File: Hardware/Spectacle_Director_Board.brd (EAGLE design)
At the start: 25.4 x 55.9 mm, 57 parts, among them J1 AUDIO-JACK3, J2 CORTEX_DEBUGPTH, Q1 2N7002PW, Q2 2N7002PW, U3 AP2112K-3.3V, U4 ATSAMD21G-A, U5 W25Q32FVSS

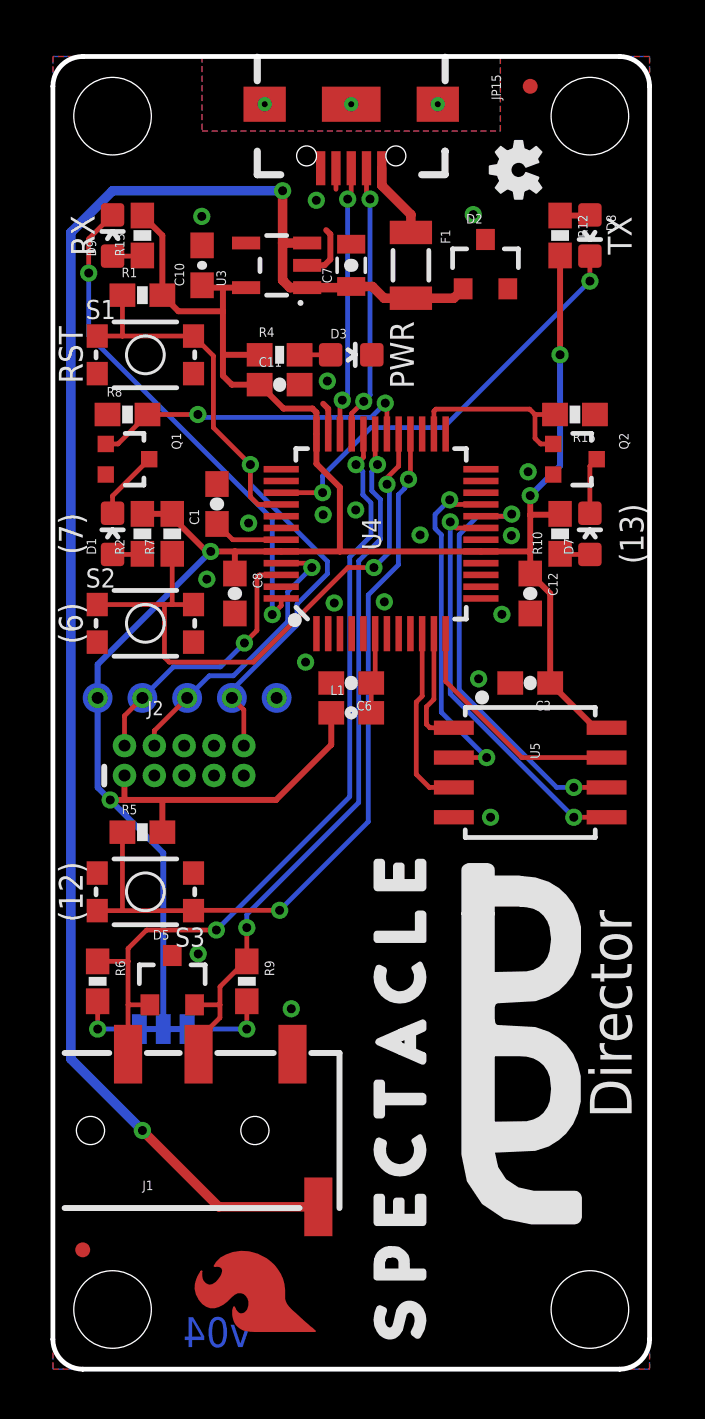
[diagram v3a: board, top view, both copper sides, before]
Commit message: Adding second trrs for program, usb out control
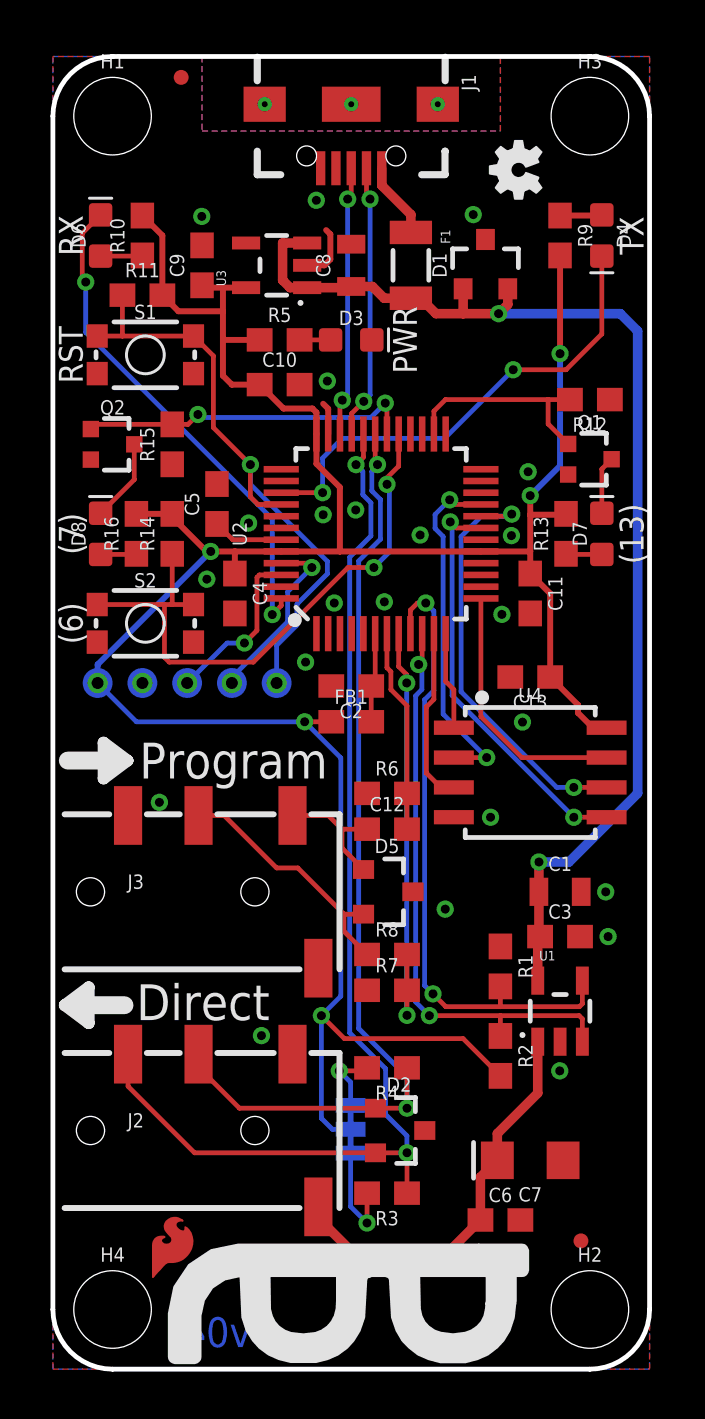
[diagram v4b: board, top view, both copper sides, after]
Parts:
- removed D9: Yellow, SparkFun-LED:LED-0603
- removed JP15: (no value), SparkFun-Connectors:USB-B-MICRO-SMD_V03
- removed JP2: JUMPER-SMT_3_2-NC_TRACE_SILK, SparkFun-Jumpers:SMT-JUMPER_3_2-NC_TRACE_SILK
- removed L1: FB - 30Ohm, SparkFun-Passives:0603
- removed S3: BTN1, SparkFun-Electromechanical:TACTILE_SWITCH_SMD_4.6X2.8MM
- removed U5: W25Q32FVSS, SparkFun-DigitalIC:SOIC-8
- added C13, C3, C4, C5: 0.1uF, SparkFun-Capacitors:0603
- added C9: 2.2uF, SparkFun-Capacitors:0603
- added D4: GREEN, SparkFun-LED:LED-0603
- added D6: Yellow, SparkFun-LED:LED-0603
- added FB1: 30Ω/1.8A, SparkFun-Inductors:0603
- added J3: Serial-TRRS, SparkFun-Connectors:AUDIO_JACK_3.5MM_TRRS_SMD_RA
- added JP1: JUMPER-SMT_3_2-NC_TRACE_SILK, SparkFun-Jumpers:SMT-JUMPER_3_2-NC_TRACE_SILK
- added R11, R14: 10k, SparkFun-Resistors:0603
- added R16: 330, SparkFun-Resistors:0603
- added R3: 2.2k, SparkFun-Resistors:0603
- added U1: AP2151, spectacle-director-temp:SOT23-5
- added U2: ATSAMD21G-A, SparkFun-IC-Microcontroller:TQFP-48
- C1: value 0.1uF -> 10uF; device SparkFun-Capacitors:0603-CAP -> SparkFun-Capacitors:0805
- C10: value 2.2uF -> 0.1uF; device SparkFun-Capacitors:0603-CAP@1 -> SparkFun-Capacitors:0603
- C11, C2, C6: device SparkFun-Capacitors:0603-CAP -> SparkFun-Capacitors:0603
- C12: value 0.1uF -> 1.0uF; device SparkFun-Capacitors:0603-CAP -> SparkFun-Capacitors:0603
- C7: value 1.0uF -> 10uF; device SparkFun-Capacitors:0805-CAP -> SparkFun-Capacitors:EIA3216
- C8: value 0.1uF -> 1.0uF; device SparkFun-Capacitors:0603-CAP -> SparkFun-Capacitors:0805
- D1: value GREEN -> PESD1CAN; device SparkFun-LED:LED-0603 -> SparkFun-DiscreteSemi:SOT23-3
- FD1, FD2: device SparkFun-Aesthetics:MICRO-FIDUCIAL -> SparkFun-Aesthetics:FIDUCIAL-MICRO
- H1, H2, H3, H4: device SparkFun-Electromechanical:STAND-OFF -> SparkFun-Hardware:STAND-OFF
- J1: value AUDIO-JACK3 -> (none); device SparkFun-Connectors:AUDIO-JACK-TRRS-SMD -> SparkFun-Connectors:USB-B-MICRO-SMD
- J2: value CORTEX_DEBUGPTH -> I2C-TRRS; device SparkFun-Connectors:2X5-PTH-1.27MM -> SparkFun-Connectors:AUDIO_JACK_3.5MM_TRRS_SMD_RA
- LOGO1: value SFE_LOGO_NAME.2_INCH -> OSHW-LOGOMINI; device SparkFun-Aesthetics:SFE_LOGO_NAME_.2 -> SparkFun-Aesthetics:OSHW-LOGO-MINI
- LOGO2: value OSHW-LOGOMINI -> SFE_LOGO_NAME.2_INCH; device SparkFun-Aesthetics:OSHW-LOGO-MINI -> SparkFun-Aesthetics:SFE_LOGO_NAME_.2
- LOGO3: value SFE_LOGO_FLAME.2EXP -> SFE_LOGO_FLAME.1COP; device SparkFun-Aesthetics:SFE_LOGO_FLAME_COPPER_EXPOSED_.2 -> SparkFun-Aesthetics:SFE_LOGO_FLAME_COPPER_.1
- Q1, Q2: value 2N7002PW -> 310mA/60V/1.6Ω
- R1: value 10K -> 100k; device SparkFun-Resistors:0603-RES -> SparkFun-Resistors:0603
- R10, R13, R15: device SparkFun-Resistors:0603-RES -> SparkFun-Resistors:0603
- R12: value 330 -> 100k; device SparkFun-Resistors:0603-RES -> SparkFun-Resistors:0603
- R2: value 330 -> 10k; device SparkFun-Resistors:0603-RES -> SparkFun-Resistors:0603
- R4: value 1K -> 2.2k; device SparkFun-Resistors:0603-RES@1 -> SparkFun-Resistors:0603
- R5: value 10K -> 1k; device SparkFun-Resistors:0603-RES -> SparkFun-Resistors:0603
- R6: value 2.2k -> 4.7k; device SparkFun-Resistors:0603-RES@1 -> SparkFun-Resistors:0603
- R7: value 10K -> DNP; device SparkFun-Resistors:0603-RES -> SparkFun-Resistors:0603
- R8: value 100k -> 0; device SparkFun-Resistors:0603-RES -> SparkFun-Resistors:0603
- R9: value 2.2k -> 330; device SparkFun-Resistors:0603-RES@1 -> SparkFun-Resistors:0603
- S1, S2: device SparkFun-Electromechanical:TACTILE_SWITCH_SMD_4.6X2.8MM -> SparkFun-Switches:TACTILE_SWITCH_SMD_4.6X2.8MM
- U3: value AP2112K-3.3V -> 3.3V; device SparkFun-PowerIC:SOT23-5 -> SparkFun-IC-Power:SOT23-5
- U4: value ATSAMD21G-A -> W25Q32FV; device samd21-temp:TQFP-48 -> SparkFun-IC-Memory:SOIC-8
- moved H1 50.8 mm to (2.54, 53.3)
- moved H2 50.8 mm to (22.9, 2.54)
- moved H3 50.8 mm to (22.9, 53.3)
- moved H4 50.8 mm to (2.54, 2.54)
- moved FD1 50.1 mm to (5.46, 55.0)
- moved FD2 49.2 mm to (22.5, 5.46)
- moved J1 45.5 mm to (12.7, 53.8), turned to 270 degrees
- moved C7 38.9 mm to (20.3, 8.89), turned to 180 degrees
- moved D2 37.0 mm to (14.7, 10.2), turned to 270 degrees
- moved R9 34.4 mm to (21.6, 48.3)
- moved R1 32.4 mm to (19.1, 17.1), turned to 270 degrees
- moved R4 30.7 mm to (14.2, 12.8), turned to 180 degrees
- moved LOGO2 28.3 mm to (23.6, 23.0), flipped to the bottom, turned to 0 degrees
- moved R2 26.9 mm to (19.1, 13.3), turned to 270 degrees
- moved R8 25.5 mm to (14.2, 17.7)
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- renumbered FRAME2 to FRAME1
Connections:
- removed net A4_FLASH!WP!: U4.10, U5.3
- removed net D10: U4.27
- removed net D12_BTN1: R5.1, S3.3, S3.4, U4.28
- removed net D6_BTN2: R7.1, S2.3, S2.4, U4.29
- removed net D8_FLASH!CS!: U4.11, U5.1
- removed net D9_FLASH!HD!: U4.12, U5.7
- new net A1_FSK-RX: C12.2, R6.2, U2.7
- new net A2: R7.2, R8.2, U2.8
- new net A3_VOUT_EN: R1.2, U1.4, U2.9
- new net A4_VOUT_FLG: R2.1, U1.3, U2.10
- new net D4_FLASH!HD!: U2.13, U4.7
- new net D6_BTN: R14.1, S2.3, S2.4, U2.29
- new net D8_FLASH!WP!: U2.11, U4.3
- new net D9_FLASH!CS!: U2.12, U4.1
- new net RING1-RIGHT: D5.2, J3.RING1, R8.1
- new net TIP-LEFT: C12.1, D5.1, J3.TIP
- new net VOUT: C6.1, C7.+, J2.EARTH, U1.1
- net !RESET: now also R11.1, U2.40; no longer J2.10, R1.1, U4.40
- net 3.3V: now also C13.1, C4.1, C9.1, FB1.1, JP1.2, R11.2, R14.2, R16.2, R5.1, R9.2, U2.17, U2.36, U2.44, U4.8; no longer C12.1, C2.1, C8.1, J2.1, JP2.2, L1.1, R1.2, R12.2, R4.1, R5.2, R7.2, U4.17, U4.36, U4.44, U5.8
- net D13_LED1: now also Q1.1, R12.2, U2.26; no longer Q2.1, R15.2, U4.26
- net D7_LED2: now also Q2.1, R15.2, U2.30; no longer Q1.1, R8.2, U4.30
- net GND: now also C13.2, C3.2, C4.2, C5.2, C7.-, C9.2, D1.3, J1.GND, J2.TIP, J3.EARTH, J3.RING2, R1.1, R12.1, R6.1, R7.1, U1.2, U2.18, U2.35, U2.42, U2.5, U4.4; no longer C12.2, C7.2, J1.TIP, J2.3, J2.5, JP15.GND, R8.1, S3.1, S3.2, U4.18, U4.35, U4.42, U4.5, U5.4
- net N$1: now also D8.A, R16.1; no longer D1.A, R2.1
- net N$10: now also Q1.3; no longer Q2.3
- net N$11: now also D4.A, R9.1; no longer D8.A, R12.1
- net N$12: now also D6.A, R10.1; no longer D9.A, R13.1
- net N$2: now also R5.2; no longer R4.2
- net N$4: now also JP1.3, R3.2; no longer JP2.3, R6.2
- net N$5: now also JP1.1, R4.2; no longer JP2.1, R9.2
- net N$7: now also D8.C, Q2.3; no longer D1.C, Q1.3
- net N$9: now also R13.1; no longer R10.1
- net RX_LED: now also D6.C, U2.48; no longer D9.C, U4.48
- net SCL: now also D2.2, J2.RING2, R3.1, U2.32; no longer D5.1, J1.RING2, R6.1, U4.32
- net SDA: now also D2.1, J2.RING1, R4.1, U2.31; no longer D5.2, J1.RING1, R9.1, U4.31
- net SHIELD: now also J1.SHIELD1, J1.SHIELD2, J1.SHIELD3; no longer JP15.SHIELD1, JP15.SHIELD2, JP15.SHIELD3
- net SPI_MISO: now also U2.21, U4.2; no longer U4.21, U5.2
- net SPI_MOSI: now also U2.19, U4.5; no longer U4.19, U5.5
- net SPI_SCK: now also U2.20, U4.6; no longer U4.20, U5.6
- net SWCLK: now also U2.45; no longer J2.4, U4.45
- net SWDIO: now also U2.46; no longer J2.2, U4.46
- net TX_LED: now also D4.C, U2.39; no longer D8.C, U4.39
- net USB_D+: now also J1.D+, U2.34; no longer JP15.D+, U4.34
- net USB_D-: now also J1.D-, U2.33; no longer JP15.D-, U4.33
- net USB_ID: now also J1.ID; no longer JP15.ID
- net VDDANA: now also C2.1, FB1.2, U2.6; no longer C6.1, L1.2, U4.6
- net VDDCORE: now also C5.1, U2.43; no longer C1.1, U4.43
- net VUSB: now also J1.VBUS; no longer JP15.VBUS
- net V_USB: now also C1.1, C3.1, C8.1, D1.1, D1.2, U1.5; no longer C7.1, D2.1, J1.EARTH
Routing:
- net D12_BTN1: track 33.7 -> 0.00 mm, vias 2 -> 0
- net A3_VOUT_EN: track 0.00 -> 27.4 mm, vias 0 -> 2
- net D6_BTN2: track 25.6 -> 0.00 mm, vias 2 -> 0
- net D6_BTN: track 0.00 -> 25.6 mm, vias 0 -> 2
- net A4_VOUT_FLG: track 0.00 -> 25.1 mm, vias 0 -> 2
- net V_USB: track 71.1 -> 51.2 mm
- net A2: track 0.00 -> 19.0 mm, vias 0 -> 2
- net VOUT: track 0.00 -> 17.1 mm
- net SCL: track 35.0 -> 48.5 mm
- net D4_FLASH!HD!: track 0.00 -> 11.1 mm
- net SDA: track 31.0 -> 42.1 mm
- net RING1-RIGHT: track 0.00 -> 10.9 mm
- net D9_FLASH!HD!: track 10.2 -> 0.00 mm
- net 3.3V: track 104.4 -> 113.6 mm, vias 5 -> 6
- net A1_FSK-RX: track 0.00 -> 8.68 mm
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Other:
- outline, holes or cut-outs redrawn
- board text added: "Direct"
- board text added: "Program"
- board text removed: "(12)"
- board text removed: "Director"
